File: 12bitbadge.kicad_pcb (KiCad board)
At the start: 2 copper layers, 62.6 x 53.7 mm, 44 parts, among them J1 Conn_02x04_Counter_Clockwise, J2 Conn_02x04_Counter_Clockwise, J3 Conn_02x04_Counter_Clockwise, J4 Conn_02x03_Odd_Even, J5 Conn_02x03_Odd_Even, J6 Conn_02x03_Odd_Even, J7 Conn_02x03_Odd_Even, SW1 SW_SPDT, SW10 SW_SPDT, SW11 SW_SPDT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

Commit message: Small routing tweaks
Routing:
- net (no net): track 0.18 -> 7.36 mm, vias 0 -> 4
- net 0V: track 66.6 -> 70.2 mm, vias 13 -> 15
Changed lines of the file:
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@@
     (thickness 1.6)
     (drawings 6)
-    (tracks 382)
+    (tracks 391)
     (zones 0)
     (modules 44)
@@
   (gr_line (start 191.897 90.297) (end 191.897 36.576) (layer Edge.Cuts) (width 0.05))
   (segment (start 166.88 55.8) (end 166.88 55.624) (width 0.2) (layer B.Cu) (net 0))
-  (via (at 181.991 46.101) (size 0.8) (drill 0.4) (layers F.Cu B.Cu) (net 5))
+  (segment (start 182.753 46.736) (end 185.293 44.196) (width 0.5) (layer F.Cu) (net 0))
+  (via (at 182.753 46.736) (size 0.8) (drill 0.4) (layers F.Cu B.Cu) (net 0))
+  (via (at 185.293 44.196) (size 0.8) (drill 0.4) (layers F.Cu B.Cu) (net 0))
+  (segment (start 181.229 45.339) (end 183.769 42.799) (width 0.5) (layer F.Cu) (net 0))
+  (via (at 181.229 45.339) (size 0.8) (drill 0.4) (layers F.Cu B.Cu) (net 0))
+  (via (at 183.769 42.799) (size 0.8) (drill 0.4) (layers F.Cu B.Cu) (net 0))
   (segment (start 147.165 60.325) (end 147.6525 60.325) (width 0.2) (layer F.Cu) (net 1))
   (segment (start 142.267 60.325) (end 147.165 60.325) (width 0.2) (layer F.Cu) (net 1))
@@
   (segment (start 146.588 65.405) (end 147.731 66.548) (width 0.2) (layer F.Cu) (net 4))
   (segment (start 141.732 65.405) (end 146.588 65.405) (width 0.2) (layer F.Cu) (net 4))
+  (via (at 181.991 46.101) (size 0.8) (drill 0.4) (layers F.Cu B.Cu) (net 5))
   (via (at 186.182 76.962) (size 0.8) (drill 0.4) (layers F.Cu B.Cu) (net 5))
   (segment (start 185.082 76.962) (end 186.182 76.962) (width 0.5) (layer F.Cu) (net 5))
@@
   (segment (start 180.51 51.562) (end 179.451 51.562) (width 0.5) (layer F.Cu) (net 5))
   (via (at 184.531 43.561) (size 0.8) (drill 0.4) (layers F.Cu B.Cu) (net 5))
-  (segment (start 181.991 46.101) (end 184.531 43.561) (width 0.5) (layer F.Cu) (net 5))
+  (segment (start 181.991 46.101) (end 184.531 43.561) (width 2) (layer F.Cu) (net 5))
   (via (at 180.848 57.277) (size 0.8) (drill 0.4) (layers F.Cu B.Cu) (net 5))
   (segment (start 179.578 57.3255) (end 180.7995 57.3255) (width 0.5) (layer F.Cu) (net 5))
@@
   (segment (start 179.451 71.628) (end 180.975 70.104) (width 0.5) (layer F.Cu) (net 5))
   (segment (start 179.451 76.962) (end 179.451 71.628) (width 0.5) (layer F.Cu) (net 5))
+  (segment (start 174.117 0) (end 176.657 -2.54) (width 0.5) (layer F.Cu) (net 5))
+  (via (at 174.117 0) (size 0.8) (drill 0.4) (layers F.Cu B.Cu) (net 5))
+  (via (at 176.657 -2.54) (size 0.8) (drill 0.4) (layers F.Cu B.Cu) (net 5))
   (segment (start 189.318989 47.609989) (end 190.766 49.057) (width 0.2) (layer F.Cu) (net 8))
   (segment (start 184.251009 47.609989) (end 189.318989 47.609989) (width 0.2) (layer F.Cu) (net 8))
@@
   (segment (start 190.766 54.067) (end 190.080999 54.752001) (width 0.2) (layer F.Cu) (net 10))
   (segment (start 190.766 53.467) (end 190.766 54.067) (width 0.2) (layer F.Cu) (net 10))
-  (segment (start 190.766 65.151) (end 188.938002 65.151) (width 0.2) (layer F.Cu) (net 17))
   (segment (start 190.803998 52.197) (end 188.976 52.197) (width 0.2) (layer F.Cu) (net 11))
   (segment (start 188.661 52.512) (end 187.282 52.512) (width 0.2) (layer F.Cu) (net 11))
@@
   (segment (start 190.080999 67.706001) (end 182.225001 67.706001) (width 0.2) (layer F.Cu) (net 16))
   (segment (start 190.766 66.421) (end 190.766 67.021) (width 0.2) (layer F.Cu) (net 16))
+  (segment (start 190.766 65.151) (end 188.938002 65.151) (width 0.2) (layer F.Cu) (net 17))
   (segment (start 188.623002 65.466) (end 187.282 65.466) (width 0.2) (layer F.Cu) (net 17))
   (segment (start 188.938002 65.151) (end 188.623002 65.466) (width 0.2) (layer F.Cu) (net 17))

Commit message: Removed errant trace above sheet
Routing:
- net (no net): track 7.36 -> 0.18 mm, vias 4 -> 0
- net 0V: track 70.2 -> 73.8 mm, vias 15 -> 17
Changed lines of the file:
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@@
     (thickness 1.6)
     (drawings 6)
-    (tracks 391)
+    (tracks 388)
     (zones 0)
     (modules 44)
@@
   (gr_line (start 191.897 90.297) (end 191.897 36.576) (layer Edge.Cuts) (width 0.05))
   (segment (start 166.88 55.8) (end 166.88 55.624) (width 0.2) (layer B.Cu) (net 0))
-  (segment (start 182.753 46.736) (end 185.293 44.196) (width 0.5) (layer F.Cu) (net 0))
-  (via (at 182.753 46.736) (size 0.8) (drill 0.4) (layers F.Cu B.Cu) (net 0))
-  (via (at 185.293 44.196) (size 0.8) (drill 0.4) (layers F.Cu B.Cu) (net 0))
-  (segment (start 181.229 45.339) (end 183.769 42.799) (width 0.5) (layer F.Cu) (net 0))
-  (via (at 181.229 45.339) (size 0.8) (drill 0.4) (layers F.Cu B.Cu) (net 0))
-  (via (at 183.769 42.799) (size 0.8) (drill 0.4) (layers F.Cu B.Cu) (net 0))
+  (segment (start 182.753 46.736) (end 185.293 44.196) (width 0.5) (layer F.Cu) (net 5))
+  (via (at 182.753 46.736) (size 0.8) (drill 0.4) (layers F.Cu B.Cu) (net 5))
+  (via (at 185.293 44.196) (size 0.8) (drill 0.4) (layers F.Cu B.Cu) (net 5))
+  (segment (start 181.229 45.339) (end 183.769 42.799) (width 0.5) (layer F.Cu) (net 5))
+  (via (at 181.229 45.339) (size 0.8) (drill 0.4) (layers F.Cu B.Cu) (net 5))
+  (via (at 183.769 42.799) (size 0.8) (drill 0.4) (layers F.Cu B.Cu) (net 5))
   (segment (start 147.165 60.325) (end 147.6525 60.325) (width 0.2) (layer F.Cu) (net 1))
   (segment (start 142.267 60.325) (end 147.165 60.325) (width 0.2) (layer F.Cu) (net 1))
@@
   (segment (start 179.451 71.628) (end 180.975 70.104) (width 0.5) (layer F.Cu) (net 5))
   (segment (start 179.451 76.962) (end 179.451 71.628) (width 0.5) (layer F.Cu) (net 5))
-  (segment (start 174.117 0) (end 176.657 -2.54) (width 0.5) (layer F.Cu) (net 5))
-  (via (at 174.117 0) (size 0.8) (drill 0.4) (layers F.Cu B.Cu) (net 5))
-  (via (at 176.657 -2.54) (size 0.8) (drill 0.4) (layers F.Cu B.Cu) (net 5))
   (segment (start 189.318989 47.609989) (end 190.766 49.057) (width 0.2) (layer F.Cu) (net 8))
   (segment (start 184.251009 47.609989) (end 189.318989 47.609989) (width 0.2) (layer F.Cu) (net 8))

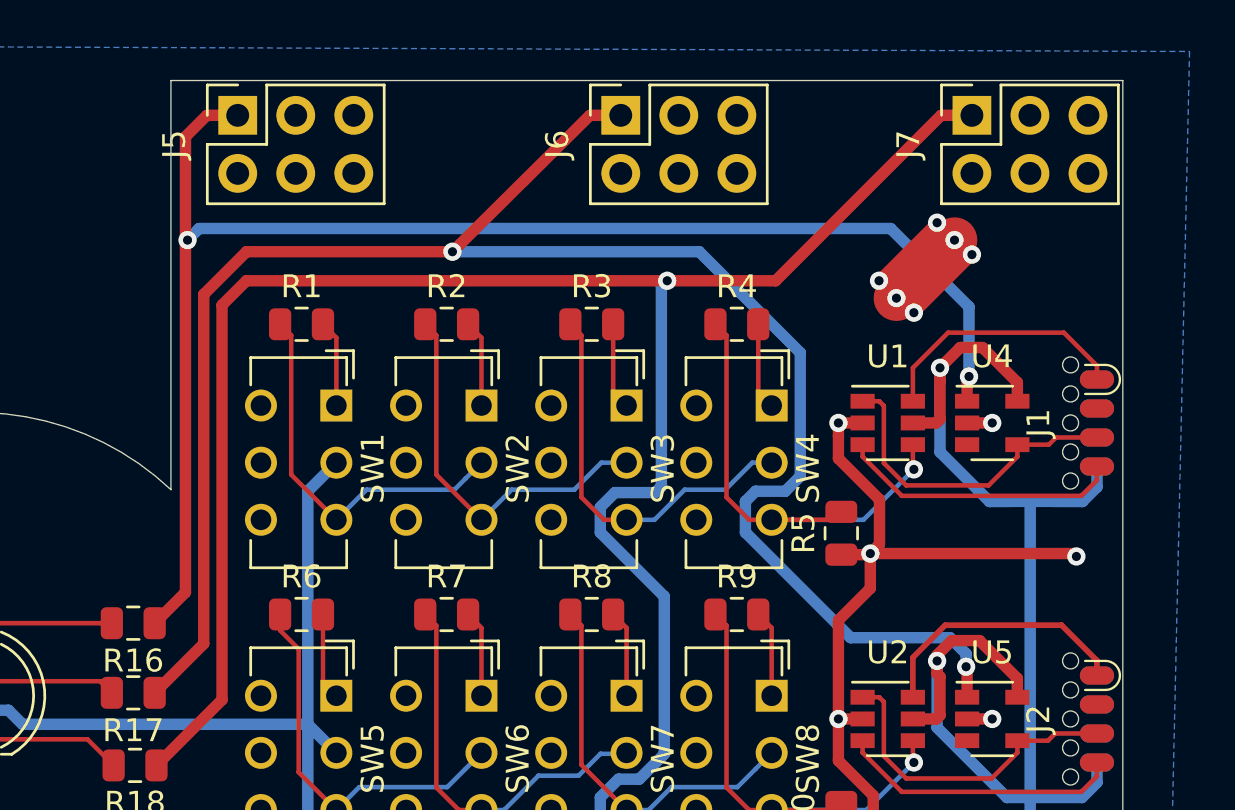
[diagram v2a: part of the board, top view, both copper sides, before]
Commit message: Put the add-on add-onsat a more rakish angle
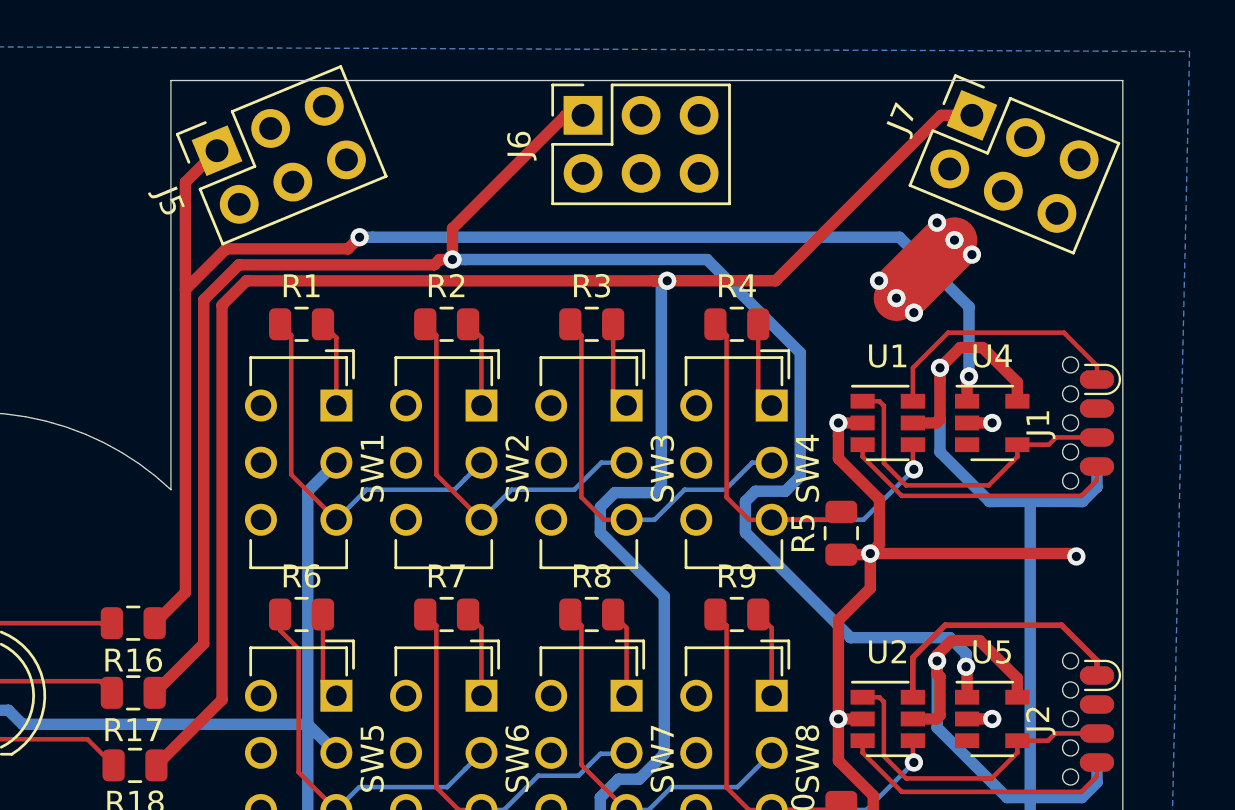
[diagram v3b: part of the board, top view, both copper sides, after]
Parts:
- moved J5 1.79 mm to (152.3, 39.6), turned to 112.5 degrees
- moved J6 1.65 mm to (168.3, 38.1)
- turned J7 to 67.5 degrees
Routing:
- net PWR_OUT_1: track 64.5 -> 62.5 mm
- net PWR_OUT_2: track 80.4 -> 79.1 mm

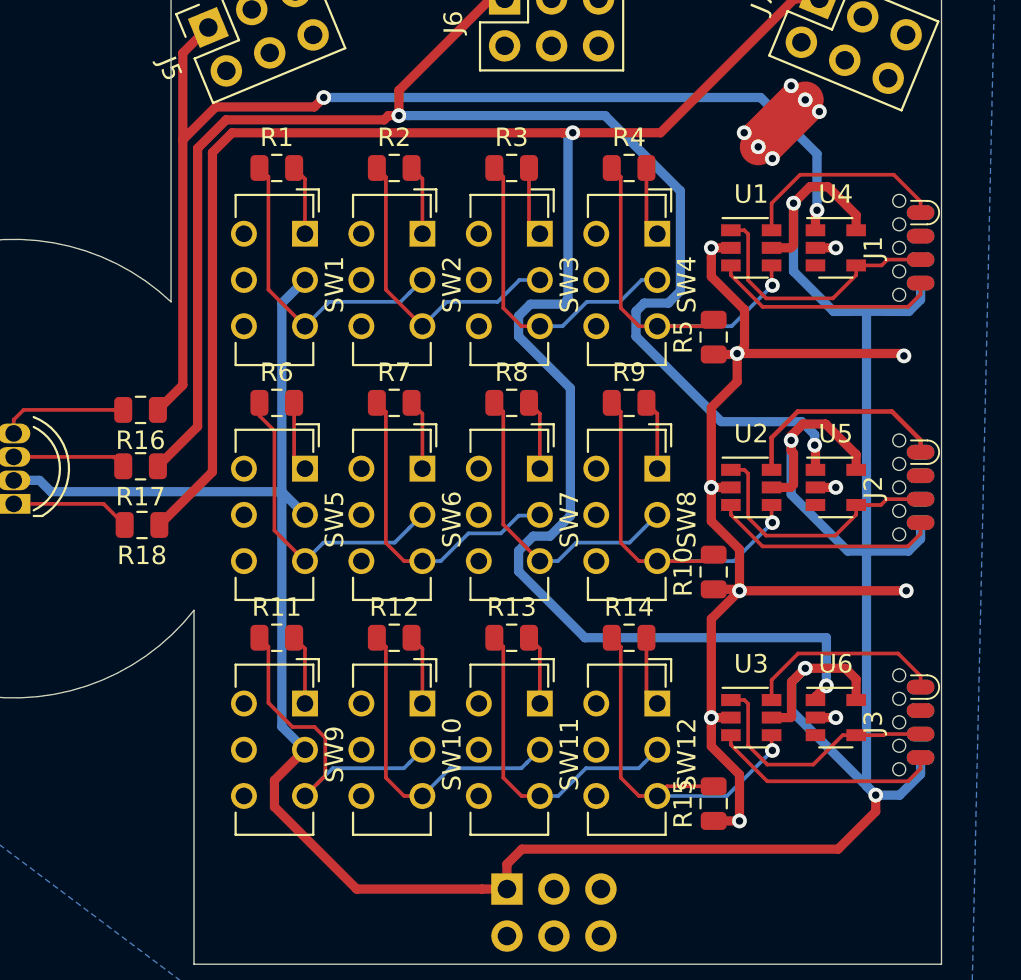
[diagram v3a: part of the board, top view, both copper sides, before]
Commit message: Updated to hand-solderable SMD
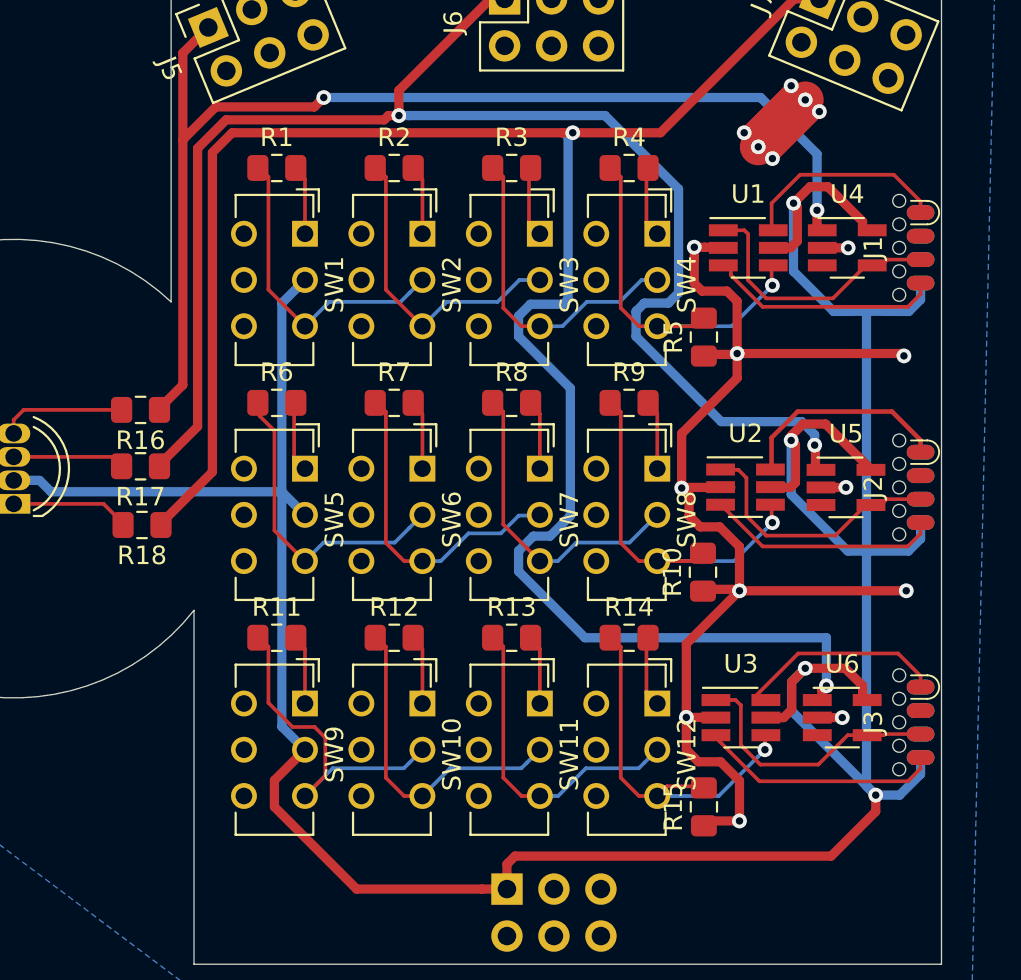
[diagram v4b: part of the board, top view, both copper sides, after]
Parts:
- R1, R10, R11, R12, R13, R14, R15, R16, R17, R18, R2, R3, R4, R5, R6, R7, R8, R9: footprint Resistor_SMD:R_0805_2012Metric -> Resistor_SMD:R_0805_2012Metric_Pad1.15x1.40mm_HandSolder
- U1, U2, U3: footprint Package_TO_SOT_SMD:SOT-23-6 -> Package_TO_SOT_SMD:SOT-23-6_Handsoldering
- U4, U5, U6: footprint Package_TO_SOT_SMD:SOT-23-5 -> Package_TO_SOT_SMD:SOT-23-5_HandSoldering
- moved U4 0.62 mm to (186.8, 51.6)
- moved R10 0.58 mm to (179.0, 69.1)
- moved U3 0.56 mm to (181.1, 77.0)
- moved R15 0.56 mm to (179.1, 81.8)
- moved U5 0.55 mm to (186.7, 64.5)
- moved R5 0.53 mm to (179.1, 56.4)
- moved U6 0.35 mm to (186.5, 77.0)
- moved U2 0.31 mm to (181.3, 64.5)
- moved U1 0.16 mm to (181.4, 51.6)
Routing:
- net 0V: track 73.8 -> 81.9 mm
- net 3.3V: track 174.8 -> 176.0 mm
- net G_OUT: track 14.2 -> 13.2 mm
- net /tpi_clk_3: track 12.5 -> 13.1 mm
- net B_OUT: track 13.6 -> 14.1 mm

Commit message: Added silkscreen rosettes
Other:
- board text added: "RGB LED SAO Sam Ettinger Feb. 2020"
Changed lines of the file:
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@@
   (general
     (thickness 1.6)
-    (drawings 6)
+    (drawings 55)
     (tracks 407)
     (zones 0)
@@
     (35 F.Paste user)
     (36 B.SilkS user)
-    (37 F.SilkS user hide)
+    (37 F.SilkS user)
     (38 B.Mask user)
     (39 F.Mask user)
@@
       (psnegative false)
       (psa4output false)
-      (plotreference true)
-      (plotvalue true)
+      (plotreference false)
+      (plotvalue false)
       (plotinvisibletext false)
       (padsonsilk false)
@@
     )
   )
+  (gr_circle (center 143.9234 53.263725) (end 144.256148 55.112854) (layer F.SilkS) (width 0.12))
+  (gr_circle (center 146.498686 54.175035) (end 146.341506 56.047278) (layer F.SilkS) (width 0.12))
+  (gr_circle (center 148.750357 55.721825) (end 148.113961 57.489592) (layer F.SilkS) (width 0.12))
+  (gr_circle (center 150.524965 57.798686) (end 149.452722 59.341506) (layer F.SilkS) (width 0.12))
+  (gr_circle (center 151.701574 60.264082) (end 150.266555 61.476815) (layer F.SilkS) (width 0.12))
+  (gr_circle (center 152.2 62.95) (end 150.5 63.75) (layer F.SilkS) (width 0.12))
+  (gr_circle (center 151.986275 65.6734) (end 150.137146 66.006148) (layer F.SilkS) (width 0.12))
+  (gr_circle (center 151.074965 68.248686) (end 149.202722 68.091506) (layer F.SilkS) (width 0.12))
+  (gr_circle (center 149.528175 70.500357) (end 147.760408 69.863961) (layer F.SilkS) (width 0.12))
+  (gr_circle (center 147.451314 72.274965) (end 145.908494 71.202722) (layer F.SilkS) (width 0.12))
+  (gr_circle (center 144.985918 73.451574) (end 143.773185 72.016555) (layer F.SilkS) (width 0.12))
+  (gr_circle (center 142.3 73.95) (end 141.5 72.25) (layer F.SilkS) (width 0.12))
+  (gr_circle (center 139.5766 73.736275) (end 139.243852 71.887146) (layer F.SilkS) (width 0.12))
+  (gr_circle (center 137.001314 72.824965) (end 137.158494 70.952722) (layer F.SilkS) (width 0.12))
+  (gr_circle (center 134.749643 71.278175) (end 135.386039 69.510408) (layer F.SilkS) (width 0.12))
+  (gr_circle (center 132.975035 69.201314) (end 134.047278 67.658494) (layer F.SilkS) (width 0.12))
+  (gr_circle (center 131.798426 66.735918) (end 133.233445 65.523185) (layer F.SilkS) (width 0.12))
+  (gr_circle (center 131.3 64.05) (end 133 63.25) (layer F.SilkS) (width 0.12))
+  (gr_circle (center 131.513725 61.3266) (end 133.362854 60.993852) (layer F.SilkS) (width 0.12))
+  (gr_circle (center 132.425035 58.751314) (end 134.297278 58.908494) (layer F.SilkS) (width 0.12))
+  (gr_circle (center 133.971825 56.499643) (end 135.739592 57.136039) (layer F.SilkS) (width 0.12))
+  (gr_circle (center 136.048686 54.725035) (end 137.591506 55.797278) (layer F.SilkS) (width 0.12))
+  (gr_circle (center 138.514082 53.548426) (end 139.726815 54.983445) (layer F.SilkS) (width 0.12))
+  (gr_circle (center 140.813241 55.018551) (end 142.473582 53.651705) (layer F.SilkS) (width 0.12))
+  (gr_circle (center 143.040321 55.065098) (end 144.997853 54.174554) (layer F.SilkS) (width 0.12))
+  (gr_circle (center 145.179468 55.68647) (end 147.300788 55.332917) (layer F.SilkS) (width 0.12))
+  (gr_circle (center 147.084902 56.840321) (end 149.225446 57.047853) (layer F.SilkS) (width 0.12))
+  (gr_circle (center 148.626771 58.448019) (end 150.640665 59.202493) (layer F.SilkS) (width 0.12))
+  (gr_circle (center 149.7 60.4) (end 151.45 61.65) (layer F.SilkS) (width 0.12))
+  (gr_circle (center 150.231449 62.563241) (end 151.598295 64.223582) (layer F.SilkS) (width 0.12))
+  (gr_circle (center 150.184902 64.790321) (end 151.075446 66.747853) (layer F.SilkS) (width 0.12))
+  (gr_circle (center 149.56353 66.929468) (end 149.917083 69.050788) (layer F.SilkS) (width 0.12))
+  (gr_circle (center 148.409679 68.834902) (end 148.202147 70.975446) (layer F.SilkS) (width 0.12))
+  (gr_circle (center 146.801981 70.376771) (end 146.047507 72.390665) (layer F.SilkS) (width 0.12))
+  (gr_circle (center 144.85 71.45) (end 143.6 73.2) (layer F.SilkS) (width 0.12))
+  (gr_circle (center 142.686759 71.981449) (end 141.026418 73.348295) (layer F.SilkS) (width 0.12))
+  (gr_circle (center 140.459679 71.934902) (end 138.502147 72.825446) (layer F.SilkS) (width 0.12))
+  (gr_circle (center 138.320532 71.31353) (end 136.199212 71.667083) (layer F.SilkS) (width 0.12))
+  (gr_circle (center 136.415098 70.159679) (end 134.274554 69.952147) (layer F.SilkS) (width 0.12))
+  (gr_circle (center 134.873229 68.551981) (end 132.859335 67.797507) (layer F.SilkS) (width 0.12))
+  (gr_circle (center 133.8 66.6) (end 132.05 65.35) (layer F.SilkS) (width 0.12))
+  (gr_circle (center 133.268551 64.436759) (end 131.901705 62.776418) (layer F.SilkS) (width 0.12))
+  (gr_circle (center 133.315098 62.209679) (end 132.424554 60.252147) (layer F.SilkS) (width 0.12))
+  (gr_circle (center 133.93647 60.070532) (end 133.582917 57.949212) (layer F.SilkS) (width 0.12))
+  (gr_circle (center 135.090321 58.165098) (end 135.297853 56.024554) (layer F.SilkS) (width 0.12))
+  (gr_circle (center 136.698019 56.623229) (end 137.452493 54.609335) (layer F.SilkS) (width 0.12))
+  (gr_circle (center 138.65 55.55) (end 139.9 53.8) (layer F.SilkS) (width 0.12))
+  (gr_circle (center 141.2 53.05) (end 142 54.75) (layer F.SilkS) (width 0.12))
+  (gr_text "RGB LED SAO\nSam Ettinger\nFeb. 2020" (at 183.3 87.2) (layer F.SilkS)
+    (effects (font (size 1 1) (thickness 0.15)))
+  )
   (gr_line (start 151.480741 90.297) (end 191.897 90.297) (layer Edge.Cuts) (width 0.05))
